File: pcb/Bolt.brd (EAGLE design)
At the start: 57.6 x 42.9 mm, 58 parts, among them J1 10118194-0001LF, Q1 XT60_YELLOW, Q2 MMSS8050-H-TP, Q3 MMSS8050-H-TP, U1 FT231XS-R, U2 ESP32-WROOM-32D, U3 LM1117DT-3.3/NOPB

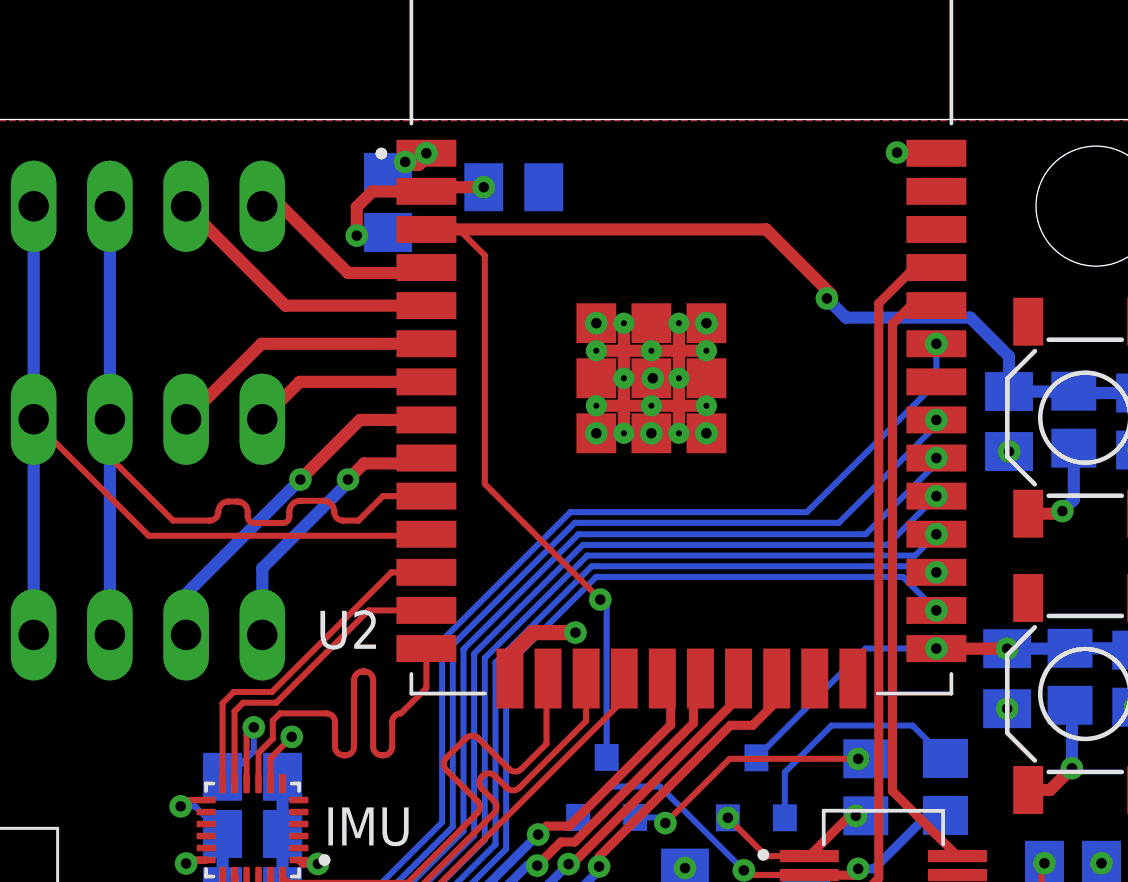
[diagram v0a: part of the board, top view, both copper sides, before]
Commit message: Fixed XSHUT routes on PCB resulting in Bolt v1.1
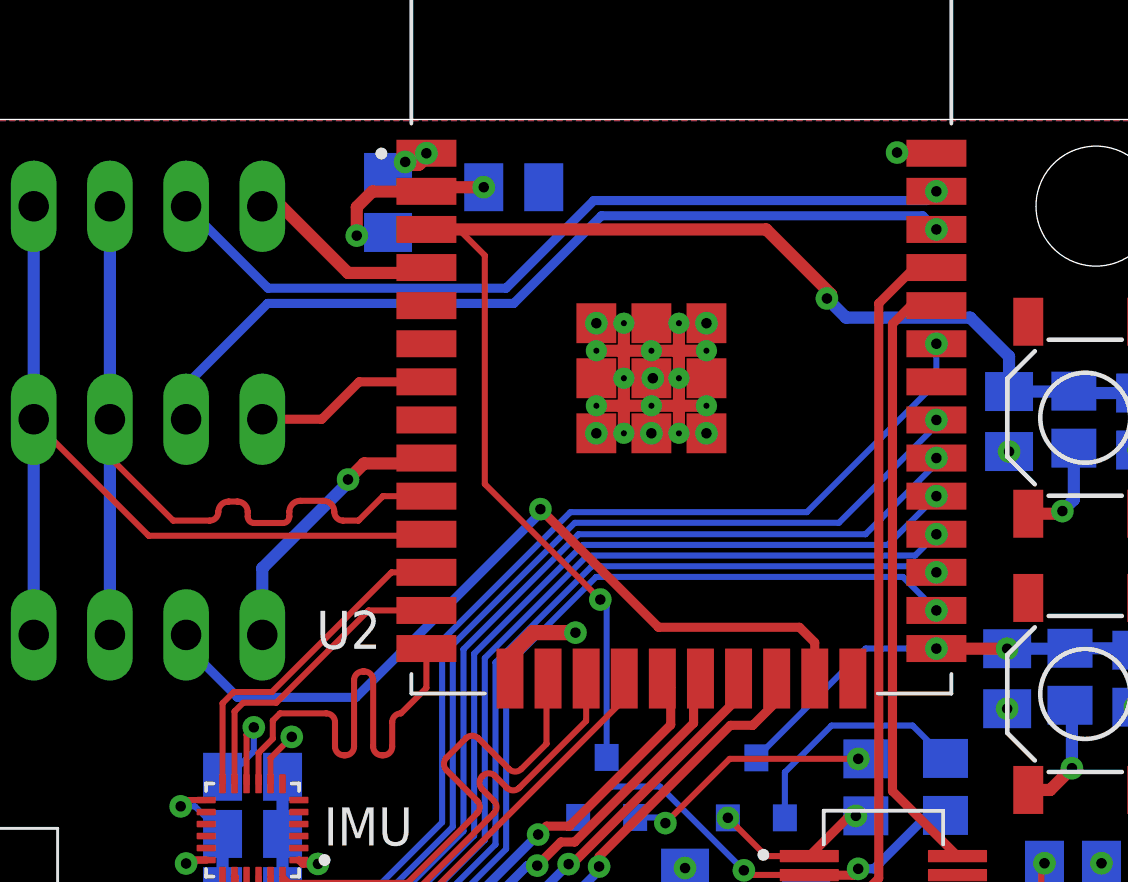
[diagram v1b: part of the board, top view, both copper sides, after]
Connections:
- net DIST_XSHUT_A: now also U2.23; no longer U2.8
- net DIST_XSHUT_B: now also U2.37; no longer U2.5
- net DIST_XSHUT_C: now also U2.36; no longer U2.6
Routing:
- net DIST_XSHUT_C: track 9.05 -> 28.7 mm, vias 0 -> 1
- net DIST_XSHUT_B: track 9.38 -> 27.5 mm, vias 0 -> 1
- net DIST_XSHUT_A: track 11.8 -> 27.7 mm
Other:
- board text added: "Bolt v1.1"
- board text removed: "Bolt v1.0"
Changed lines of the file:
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@@
 <setting verticaltext="up"/>
 </settings>
-<grid distance="10" unitdist="mil" unit="mil" style="lines" multiple="1" display="yes" altdistance="5" altunitdist="mil" altunit="mil"/>
+<grid distance="5" unitdist="mil" unit="mil" style="lines" multiple="1" display="yes" altdistance="5" altunitdist="mil" altunit="mil"/>
 <layers>
 <layer number="1" name="Top" color="4" fill="1" visible="yes" active="yes"/>
@@
 <layer number="14" name="Route14" color="22" fill="1" visible="no" active="no"/>
 <layer number="15" name="GND" color="63" fill="1" visible="no" active="yes"/>
-<layer number="16" name="Bottom" color="1" fill="1" visible="no" active="yes"/>
+<layer number="16" name="Bottom" color="1" fill="1" visible="yes" active="yes"/>
 <layer number="17" name="Pads" color="2" fill="1" visible="yes" active="yes"/>
 <layer number="18" name="Vias" color="2" fill="1" visible="yes" active="yes"/>
@@
 <text x="58.674" y="59.055" size="0.6096" layer="21">TX</text>
 <text x="58.674" y="62.103" size="0.6096" layer="21">RX</text>
-<text x="22.86" y="63.754" size="1.9304" layer="26" font="vector" ratio="12" rot="MR0">Bolt v1.0</text>
+<text x="22.86" y="63.754" size="1.9304" layer="26" font="vector" ratio="12" rot="MR0">Bolt v1.1</text>
 </plain>
 <attributes>
@@
 <signal name="DIST_XSHUT_A">
 <contactref element="DIST_A" pad="5"/>
-<contactref element="U2" pad="8"/>
-<wire x1="34.68" y1="78.92" x2="32.4662" y2="78.92" width="0.4064" layer="1"/>
-<wire x1="32.4662" y1="78.92" x2="30.48" y2="76.9338" width="0.4064" layer="1"/>
-<via x="30.48" y="76.9338" extent="1-16" drill="0.35"/>
-<wire x1="30.48" y1="76.9338" x2="26.67" y2="73.1238" width="0.4064" layer="16"/>
-<wire x1="26.67" y1="73.1238" x2="26.67" y2="71.755" width="0.4064" layer="16"/>
+<contactref element="U2" pad="23"/>
+<wire x1="47.625" y1="70.3" x2="47.625" y2="71.501" width="0.3048" layer="1"/>
+<wire x1="42.418" y1="72.009" x2="38.481" y2="75.946" width="0.3048" layer="1"/>
+<via x="38.481" y="75.946" extent="1-16" drill="0.35"/>
+<wire x1="28.3871125" y1="69.6722" x2="26.67" y2="71.3893125" width="0.3048" layer="16"/>
+<wire x1="26.67" y1="71.755" x2="26.67" y2="71.3893125" width="0.3048" layer="16"/>
+<wire x1="38.481" y1="75.946" x2="38.481" y2="75.819" width="0.3048" layer="16"/>
+<wire x1="38.481" y1="75.819" x2="32.3342" y2="69.6722" width="0.3048" layer="16"/>
+<wire x1="32.3342" y1="69.6722" x2="28.3871125" y2="69.6722" width="0.3048" layer="16"/>
+<wire x1="47.625" y1="71.501" x2="47.117" y2="72.009" width="0.3048" layer="1"/>
+<wire x1="47.117" y1="72.009" x2="42.418" y2="72.009" width="0.3048" layer="1"/>
 </signal>
 <signal name="DIST_GPIO1_A">
@@
 <signal name="DIST_XSHUT_B">
 <contactref element="DIST_B" pad="5"/>
-<contactref element="U2" pad="5"/>
-<wire x1="26.67" y1="86.0425" x2="29.9825" y2="82.73" width="0.4064" layer="1"/>
-<wire x1="29.9825" y1="82.73" x2="34.68" y2="82.73" width="0.4064" layer="1"/>
+<wire x1="26.67" y1="86.0425" x2="29.4005" y2="83.312" width="0.3048" layer="16"/>
+<wire x1="29.4005" y1="83.312" x2="37.338" y2="83.312" width="0.3048" layer="16"/>
+<contactref element="U2" pad="37"/>
+<wire x1="40.259" y1="86.233" x2="37.338" y2="83.312" width="0.3048" layer="16"/>
+<wire x1="51.373" y1="86.233" x2="40.259" y2="86.233" width="0.3048" layer="16"/>
+<wire x1="51.373" y1="86.233" x2="51.68" y2="86.54" width="0.3048" layer="16"/>
+<via x="51.68" y="86.54" extent="1-16" drill="0.35"/>
 </signal>
 <signal name="DIST_GPIO1_B">
@@
 <signal name="DIST_XSHUT_C">
 <contactref element="DIST_C" pad="5"/>
-<contactref element="U2" pad="6"/>
-<wire x1="26.67" y1="78.9432" x2="29.1868" y2="81.46" width="0.4064" layer="1"/>
-<wire x1="29.1868" y1="81.46" x2="34.68" y2="81.46" width="0.4064" layer="1"/>
+<wire x1="29.3878" y1="82.804" x2="26.67" y2="80.0862" width="0.3048" layer="16"/>
+<wire x1="26.67" y1="78.9432" x2="26.67" y2="80.0862" width="0.3048" layer="16"/>
+<contactref element="U2" pad="36"/>
+<wire x1="37.592" y1="82.804" x2="40.513" y2="85.725" width="0.3048" layer="16"/>
+<wire x1="40.513" y1="85.725" x2="51.225" y2="85.725" width="0.3048" layer="16"/>
+<wire x1="51.225" y1="85.725" x2="51.68" y2="85.27" width="0.3048" layer="16"/>
+<via x="51.68" y="85.27" extent="1-16" drill="0.35"/>
+<wire x1="29.3878" y1="82.804" x2="37.592" y2="82.804" width="0.3048" layer="16"/>
 </signal>
 <signal name="DIST_GPIO1_C">
 <contactref element="DIST_C" pad="6"/>
 <contactref element="U2" pad="7"/>
-<wire x1="29.21" y1="78.9432" x2="30.4568" y2="80.19" width="0.4064" layer="1"/>
-<wire x1="30.4568" y1="80.19" x2="34.68" y2="80.19" width="0.4064" layer="1"/>
+<wire x1="29.21" y1="78.9432" x2="31.1912" y2="78.9432" width="0.3048" layer="1"/>
+<wire x1="32.438" y1="80.19" x2="34.68" y2="80.19" width="0.3048" layer="1"/>
+<wire x1="31.1912" y1="78.9432" x2="32.438" y2="80.19" width="0.3048" layer="1"/>
 </signal>
 <signal name="HALL_1_B">
